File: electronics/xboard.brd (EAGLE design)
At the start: 78.5 x 78.5 mm, 37 parts

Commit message: Fixing consistency
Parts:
- renumbered U$10 to DC3, U$11 to DC4, U$13 to BUZZER, U$14 to DC1, U$5 to FUSE, U$6 to MOS, U$9 to DC2
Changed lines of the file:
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@@
 <element name="R3" library="rcl" package="R0805" value="20K" x="23.945059375" y="-8.123340625" rot="R180"/>
 <element name="R5" library="rcl" package="R0805" value="10K" x="27.545059375" y="-11.323340625" rot="R90"/>
-<element name="U$5" library="rhoban" package="56000001009" value="56000001009" x="-34.6968" y="7.6608"/>
-<element name="U$6" library="rhoban" package="TO252" value="SUD50N04-8M8P-4GE3" x="-20.2824" y="14.0672" rot="R90"/>
+<element name="FUSE" library="rhoban" package="56000001009" value="56000001009" x="-34.6968" y="7.6608"/>
+<element name="MOS" library="rhoban" package="TO252" value="SUD50N04-8M8P-4GE3" x="-20.2824" y="14.0672" rot="R90"/>
 <element name="R6" library="rcl" package="R0805" value="470" x="-15.7824" y="7.5672"/>
 <element name="U$7" library="rhoban" package="SOT223" value="TS2940CW-3.3RP" x="4.224928125" y="-6.2006125" rot="R180"/>
 <element name="U$8" library="rhoban" package="SOT223" value="AP1117E50G-13" x="4.3939375" y="14.40955" rot="R180"/>
 <element name="R7" library="rcl" package="R0805" value="20" x="-14.7824" y="-0.4328" rot="R90"/>
-<element name="U$9" library="rhoban" package="PANASONIC_D" value="47uF" x="18.285203125" y="10.38588125" rot="R90"/>
-<element name="U$10" library="rhoban" package="PANASONIC_D8" value="220uF" x="4.358734375" y="3.40605625"/>
-<element name="U$11" library="rhoban" package="PANASONIC_D8" value="220uF" x="4.342078125" y="23.708159375"/>
+<element name="DC2" library="rhoban" package="PANASONIC_D" value="47uF" x="18.285203125" y="10.38588125" rot="R90"/>
+<element name="DC3" library="rhoban" package="PANASONIC_D8" value="220uF" x="4.358734375" y="3.40605625"/>
+<element name="DC4" library="rhoban" package="PANASONIC_D8" value="220uF" x="4.342078125" y="23.708159375"/>
 <element name="U$12" library="rhoban" package="SOT-23" value="NPN_BC817,215" x="6.4227875" y="-24.982771875" rot="R180"/>
 <element name="R8" library="rcl" package="R0805" value="470" x="7.3511" y="-20.324259375" rot="R90"/>
-<element name="U$13" library="rhoban" package="BUZZER66" value="BUZZER66" x="-4.581790625" y="-31.34356875"/>
+<element name="BUZZER" library="rhoban" package="BUZZER66" value="BUZZER66" x="-4.581790625" y="-31.34356875"/>
 <element name="CA" library="rhoban" package="C0805" value="C_EU-100NF" x="-23.6728" y="-7.112" rot="R270">
 <attribute name="FARNELL_LINK" value="http://fr.farnell.com/kemet/c0805c104j5ractu/condensateur-100nf-50v-x7r-0805/dp/1414663RL" x="-23.6728" y="-7.112" size="1.778" layer="27" rot="R270" display="off"/>
@@
 </element>
 <element name="R9" library="rhoban" package="R0805" value="4K" x="-21.65883125" y="7.5608375"/>
-<element name="U$14" library="rhoban" package="PANASONIC_D8" value="220uF" x="4.541653125" y="31.152875"/>
+<element name="DC1" library="rhoban" package="PANASONIC_D8" value="220uF" x="4.541653125" y="31.152875"/>
 </elements>
 <signals>
@@
 <contactref element="IMU" pad="3"/>
 <contactref element="R5" pad="1"/>
-<contactref element="U$6" pad="2"/>
+<contactref element="MOS" pad="2"/>
 <contactref element="U$8" pad="1"/>
 <contactref element="U$7" pad="2"/>
-<contactref element="U$9" pad="-"/>
-<contactref element="U$10" pad="-"/>
-<contactref element="U$11" pad="-"/>
+<contactref element="DC2" pad="-"/>
+<contactref element="DC3" pad="-"/>
+<contactref element="DC4" pad="-"/>
 <contactref element="U$12" pad="2"/>
 <contactref element="CA" pad="2"/>
 <contactref element="R9" pad="1"/>
-<contactref element="U$14" pad="-"/>
+<contactref element="DC1" pad="-"/>
 <wire x1="24" y1="13.6" x2="18.4" y2="8" width="0.889" layer="1"/>
 <wire x1="24" y1="14.2" x2="24" y2="13.6" width="0.889" layer="1"/>
@@
 <contactref element="IMU" pad="2"/>
 <contactref element="U$7" pad="3"/>
-<contactref element="U$9" pad="+"/>
-<contactref element="U$13" pad="P$2"/>
+<contactref element="DC2" pad="+"/>
+<contactref element="BUZZER" pad="P$2"/>
 <wire x1="-0.2" y1="-5.2" x2="1.8" y2="-3.2" width="0.254" layer="1"/>
 <wire x1="-0.2" y1="-30.2" x2="-0.2" y2="-19.6" width="0.254" layer="1"/>
@@
 <contactref element="XL4" pad="P$2"/>
 <contactref element="R3" pad="2"/>
-<contactref element="U$5" pad="P$2"/>
-<contactref element="U$6" pad="3"/>
+<contactref element="FUSE" pad="P$2"/>
+<contactref element="MOS" pad="3"/>
 <contactref element="U$8" pad="3"/>
-<contactref element="U$11" pad="+"/>
+<contactref element="DC4" pad="+"/>
 <wire x1="-9.4" y1="17" x2="-9.4" y2="12.4" width="0.889" layer="1"/>
 <wire x1="-9.4" y1="12.4" x2="-9.475046875" y2="12.26779375" width="0.889" layer="1"/>
@@
 <contactref element="U$7" pad="1"/>
 <contactref element="U$8" pad="2"/>
-<contactref element="U$10" pad="+"/>
+<contactref element="DC3" pad="+"/>
 <contactref element="CA" pad="1"/>
 <wire x1="-21.2" y1="-6" x2="-21.8" y2="-6" width="0.254" layer="1"/>
@@
 <signal name="V+_IN" class="1">
 <contactref element="V+" pad="P$1"/>
-<contactref element="U$5" pad="P$1"/>
+<contactref element="FUSE" pad="P$1"/>
 <wire x1="-36.2" y1="6.6" x2="-37.2" y2="7.6" width="0.889" layer="1"/>
 <wire x1="-36.2" y1="0.2" x2="-36.2" y2="6.6" width="0.889" layer="1"/>
@@
 </signal>
 <signal name="N$1">
-<contactref element="U$6" pad="1"/>
+<contactref element="MOS" pad="1"/>
 <contactref element="R6" pad="1"/>
 <wire x1="-16" y1="8.2" x2="-16.6" y2="7.6" width="0.254" layer="1"/>
@@
 </signal>
 <signal name="MAPLE_VCC">
-<contactref element="U$14" pad="+"/>
+<contactref element="DC1" pad="+"/>
 <contactref element="MAPLE_MINI" pad="VCC"/>
 <wire x1="7.2" y1="34.4" x2="-3" y2="34.4" width="0.254" layer="1"/>
@@
 </signal>
 <signal name="N$5">
-<contactref element="U$13" pad="P$1"/>
+<contactref element="BUZZER" pad="P$1"/>
 <contactref element="U$12" pad="3"/>
 <wire x1="0" y1="-32.6" x2="6.4" y2="-26.2" width="0.254" layer="1"/>

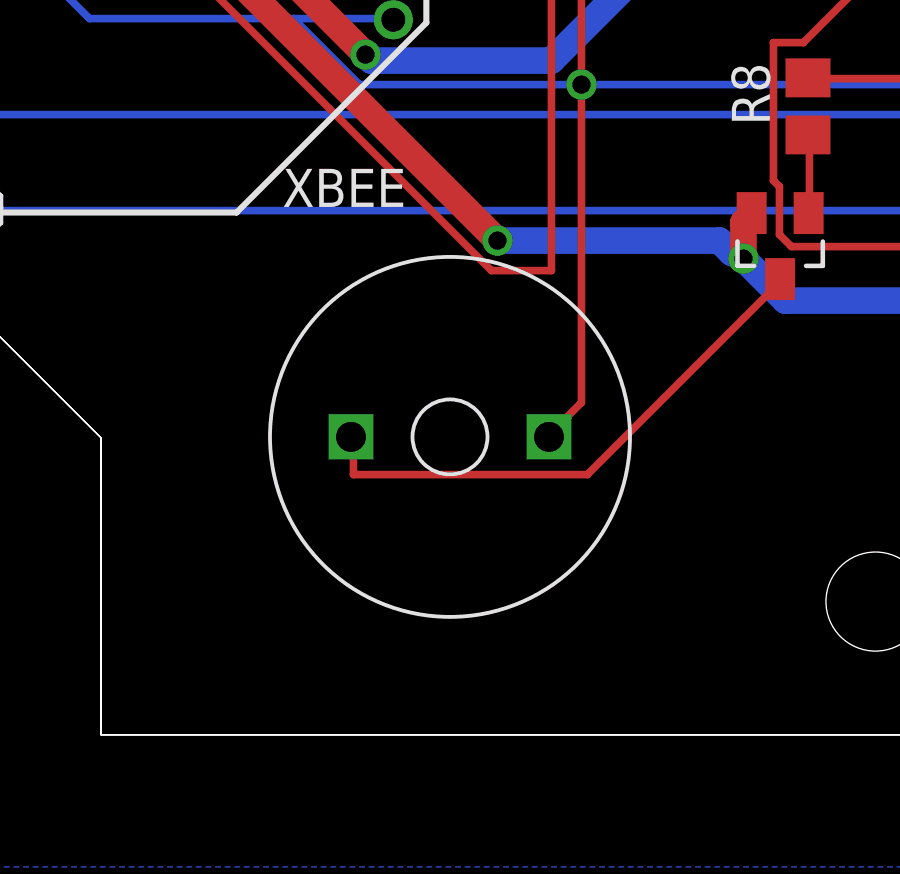
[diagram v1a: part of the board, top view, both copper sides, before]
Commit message: Buzzer 10mm
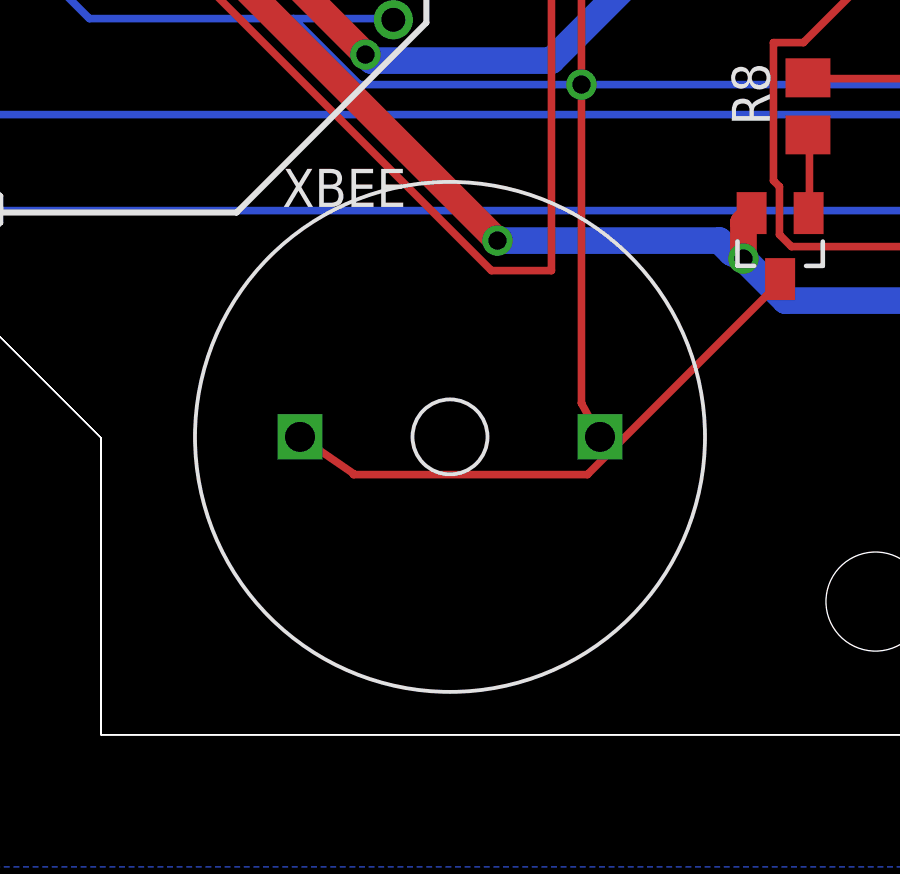
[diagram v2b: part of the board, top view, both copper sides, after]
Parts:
- BUZZER: value BUZZER66 -> BUZZER10MM; device rhoban:BUZZER66 -> rhoban:BUZZER10
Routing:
- net N$5: track 18.3 -> 19.2 mm
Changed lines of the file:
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@@
 <element name="U$12" library="rhoban" package="SOT-23" value="NPN_BC817,215" x="6.4227875" y="-24.982771875" rot="R180"/>
 <element name="R8" library="rcl" package="R0805" value="470" x="7.3511" y="-20.324259375" rot="R90"/>
-<element name="BUZZER" library="rhoban" package="BUZZER66" value="BUZZER66" x="-4.581790625" y="-31.34356875"/>
+<element name="BUZZER" library="rhoban" package="BUZZER10" value="BUZZER10MM" x="-4.581790625" y="-31.34356875"/>
 <element name="CA" library="rhoban" package="C0805" value="C_EU-100NF" x="-23.6728" y="-7.112" rot="R270">
 <attribute name="FARNELL_LINK" value="http://fr.farnell.com/kemet/c0805c104j5ractu/condensateur-100nf-50v-x7r-0805/dp/1414663RL" x="-23.6728" y="-7.112" size="1.778" layer="27" rot="R270" display="off"/>
@@
 <wire x1="-0.2" y1="-30.2" x2="-0.2" y2="-19.6" width="0.254" layer="1"/>
 <wire x1="-0.2" y1="-19.6" x2="-0.2" y2="-5.2" width="0.254" layer="1"/>
-<wire x1="-1.2" y1="-31.2" x2="-0.2" y2="-30.2" width="0.254" layer="1"/>
+<wire x1="-0.1975375" y1="-30.227915625" x2="-0.2" y2="-30.2" width="0.254" layer="1"/>
 <wire x1="1.8" y1="-3.2" x2="1.913528125" y2="-3.1018125" width="0.254" layer="1"/>
-<wire x1="-1.2" y1="-31.2" x2="-1.281790625" y2="-31.34356875" width="0.254" layer="1"/>
+<wire x1="-0.1975375" y1="-30.227915625" x2="0.418209375" y2="-31.34356875" width="0.254" layer="1"/>
 <wire x1="15" y1="9.4" x2="18.2" y2="12.6" width="0.254" layer="1"/>
 <wire x1="15" y1="1.6" x2="15" y2="9.4" width="0.254" layer="1"/>
@@
 <wire x1="0" y1="-32.6" x2="6.4" y2="-26.2" width="0.254" layer="1"/>
 <wire x1="-7.8" y1="-32.6" x2="0" y2="-32.6" width="0.254" layer="1"/>
-<wire x1="-7.8" y1="-31.4" x2="-7.8" y2="-32.6" width="0.254" layer="1"/>
+<wire x1="-7.765228125" y1="-32.59051875" x2="-7.8" y2="-32.6" width="0.254" layer="1"/>
 <wire x1="6.4" y1="-26.2" x2="6.4227875" y2="-26.082771875" width="0.254" layer="1"/>
-<wire x1="-7.8" y1="-31.4" x2="-7.881790625" y2="-31.34356875" width="0.254" layer="1"/>
+<wire x1="-7.765228125" y1="-32.59051875" x2="-9.581790625" y2="-31.34356875" width="0.254" layer="1"/>
 </signal>
 </signals>

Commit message: XBoard
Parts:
- BUZZER: value BUZZER10MM -> BUZZER66; device rhoban:BUZZER10 -> rhoban:BUZZER66
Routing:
- net N$5: track 19.2 -> 18.3 mm
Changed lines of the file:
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@@
 <element name="U$12" library="rhoban" package="SOT-23" value="NPN_BC817,215" x="6.4227875" y="-24.982771875" rot="R180"/>
 <element name="R8" library="rcl" package="R0805" value="470" x="7.3511" y="-20.324259375" rot="R90"/>
-<element name="BUZZER" library="rhoban" package="BUZZER10" value="BUZZER10MM" x="-4.581790625" y="-31.34356875"/>
+<element name="BUZZER" library="rhoban" package="BUZZER66" value="BUZZER66" x="-4.581790625" y="-31.34356875"/>
 <element name="CA" library="rhoban" package="C0805" value="C_EU-100NF" x="-23.6728" y="-7.112" rot="R270">
 <attribute name="FARNELL_LINK" value="http://fr.farnell.com/kemet/c0805c104j5ractu/condensateur-100nf-50v-x7r-0805/dp/1414663RL" x="-23.6728" y="-7.112" size="1.778" layer="27" rot="R270" display="off"/>
@@
 <wire x1="-0.1975375" y1="-30.227915625" x2="-0.2" y2="-30.2" width="0.254" layer="1"/>
 <wire x1="1.8" y1="-3.2" x2="1.913528125" y2="-3.1018125" width="0.254" layer="1"/>
-<wire x1="-0.1975375" y1="-30.227915625" x2="0.418209375" y2="-31.34356875" width="0.254" layer="1"/>
+<wire x1="-0.1975375" y1="-30.227915625" x2="-1.281790625" y2="-31.34356875" width="0.254" layer="1"/>
 <wire x1="15" y1="9.4" x2="18.2" y2="12.6" width="0.254" layer="1"/>
 <wire x1="15" y1="1.6" x2="15" y2="9.4" width="0.254" layer="1"/>
@@
 <wire x1="-7.765228125" y1="-32.59051875" x2="-7.8" y2="-32.6" width="0.254" layer="1"/>
 <wire x1="6.4" y1="-26.2" x2="6.4227875" y2="-26.082771875" width="0.254" layer="1"/>
-<wire x1="-7.765228125" y1="-32.59051875" x2="-9.581790625" y2="-31.34356875" width="0.254" layer="1"/>
+<wire x1="-7.765228125" y1="-32.59051875" x2="-7.881790625" y2="-31.34356875" width="0.254" layer="1"/>
 </signal>
 </signals>
